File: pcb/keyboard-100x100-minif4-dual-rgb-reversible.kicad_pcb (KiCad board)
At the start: 2 copper layers, 100 x 100 mm, 110 parts, among them J1 TRRS, J2 TRRS, J3 Conn_01x04_Female, M1 Motor_DC, Q1 Q_NPN_BCE, U1 BluePill_or_MiniF4_DIP40, U2 SN74LVC1T45DBV

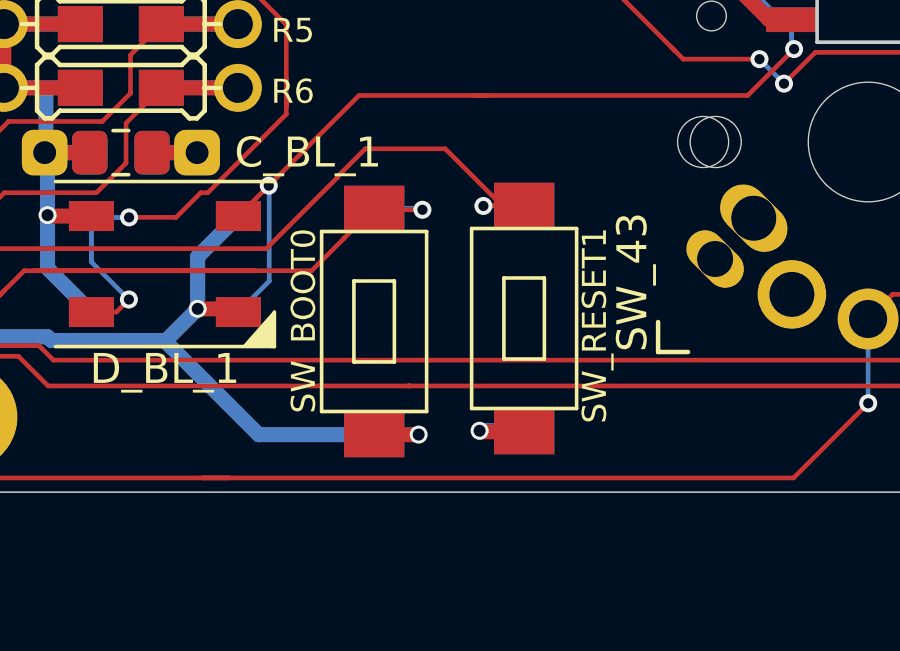
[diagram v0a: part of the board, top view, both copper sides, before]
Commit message: Kicad: refactor x-1 minif4-36 to use the reversible footprint
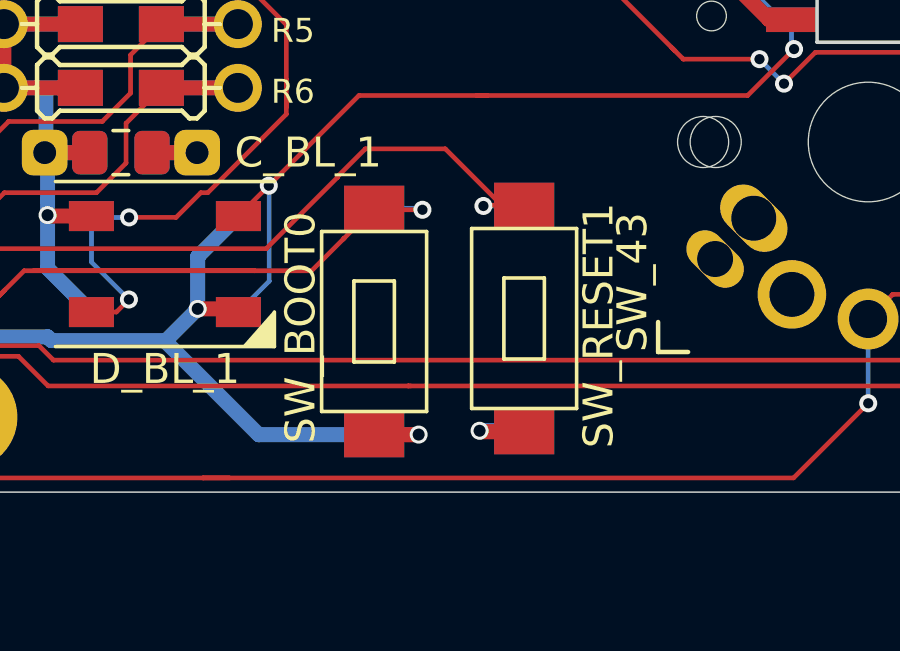
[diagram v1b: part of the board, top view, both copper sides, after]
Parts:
- SW_BOOT0, SW_RESET1: footprint ProjectLocal:SW_Push_SPST_3x6mm -> ProjectLocal:SW_Push_SPST_3x6mm_Reversible

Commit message: Kicad: minor changes to properties of X-1: MiniF4-36
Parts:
- D_11, D_12, D_13, D_14, D_15, D_21, D_22, D_23, D_24, D_25, D_31, D_32, D_33, D_34, D_35, D_41, D_42, D_43: value WS2812B -> SK6812mini-e
- H1, H2, H3, H4, H5: value MountingHole -> 3M F0502
- H10, H11, H12, H13, H6, H7, H8, H9: value MountingHole -> M2 Spacer
- J1, J2: value TRRS -> PJ-320A
- J3: value Conn_01x04_Female -> 01x04 Female Header
- M1: value Motor_DC -> 1030 or 0834
- Q1: value Q_NPN_BCE -> MMSS8050-H-TP
- SW_11, SW_12, SW_13, SW_14, SW_15, SW_21, SW_22, SW_23, SW_24, SW_25, SW_31, SW_32, SW_33, SW_34, SW_35, SW_41, SW_42, SW_43: value SW_Push -> MX-compatible or Kailh Choc v1
- SW_BOOT0, SW_RESET1: value SW_Push -> 3x6mm
- U1: value BluePill_or_MiniF4_DIP40 -> DIP-40 round-pin socket or 40-pin SIP round-pin female header (cut down to 20)

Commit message: Kicad: update fields in X-1, X-2 for U1
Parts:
- U1: value DIP-40 round-pin socket or 40-pin SIP round-pin female header (cut down to 20) -> MiniF4 STM32F4x1 "Blackpill", or Bluepill
